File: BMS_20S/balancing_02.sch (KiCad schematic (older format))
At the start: 61 parts, among them Q2001 Si2302DS, Q2002 Si2302DS, Q3403 Si2302DS, Q3404 Si2302DS, U2004 TLP290-4

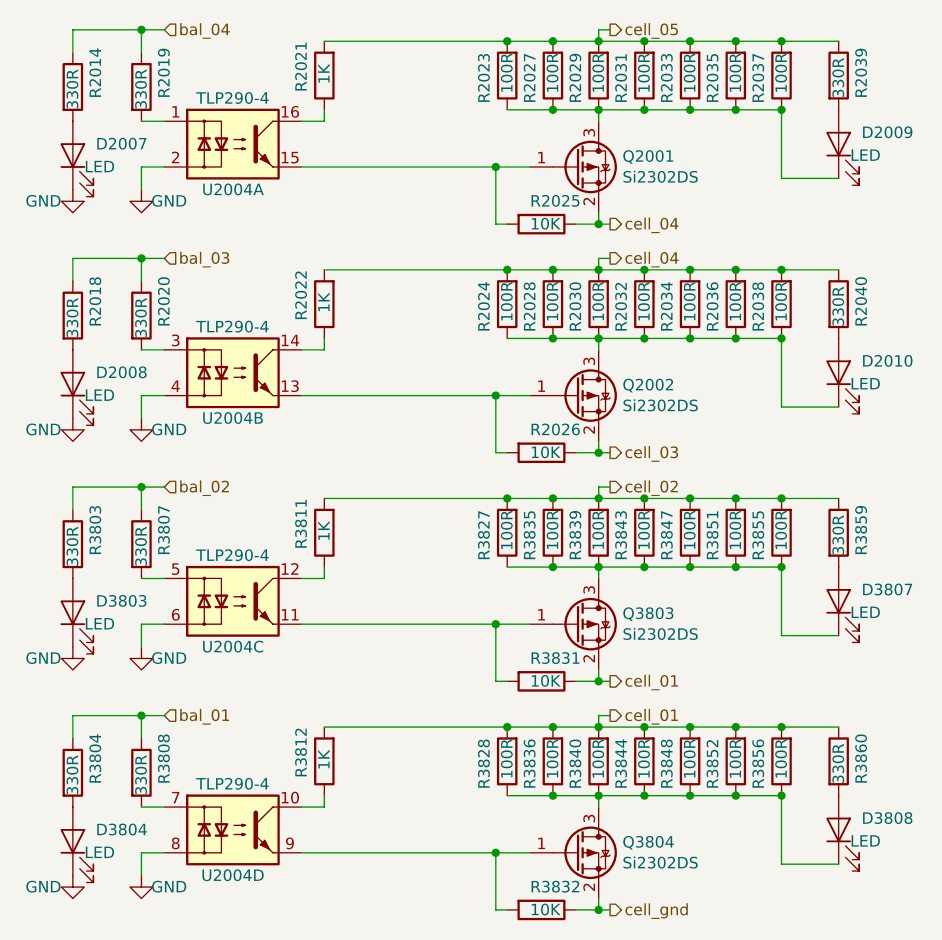
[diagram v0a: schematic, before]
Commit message: add current sense block to the schematic
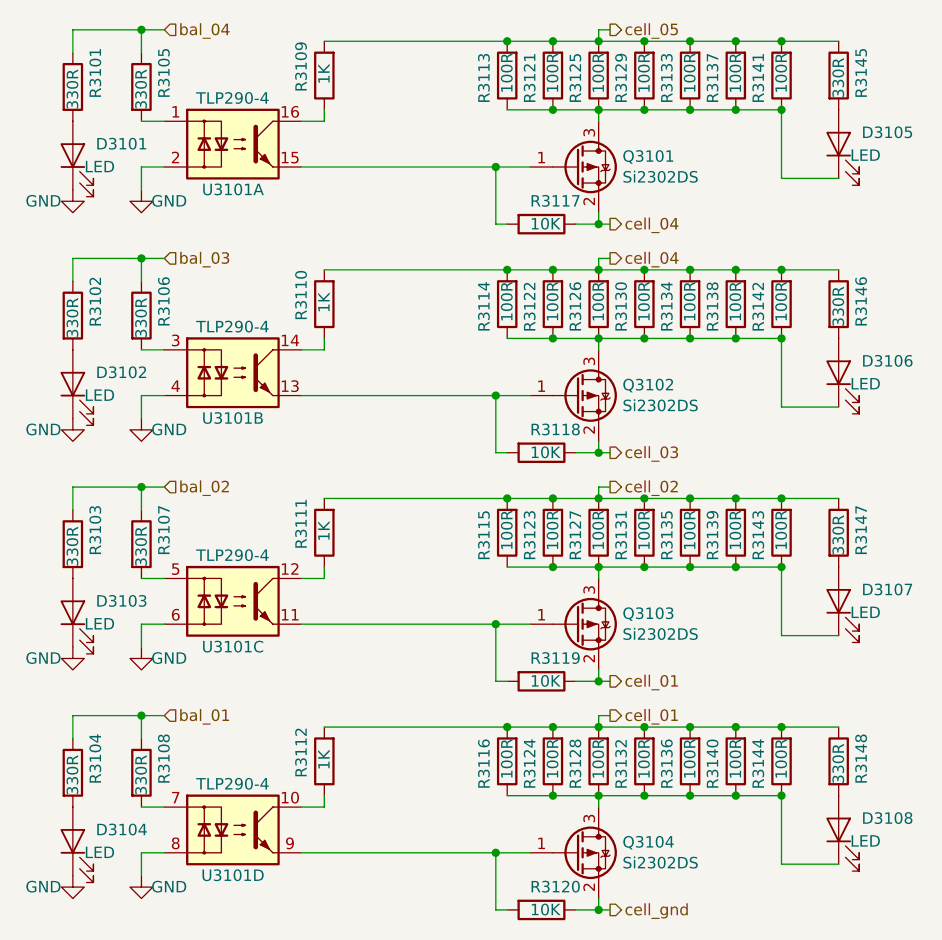
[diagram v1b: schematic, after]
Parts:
- renumbered D2007 to D3101, D2008 to D3102, D3403 to D3103, D3404 to D3104, D2009 to D3105, D2010 to D3106, D3407 to D3107, D3408 to D3108, Q2001 to Q3101, Q2002 to Q3102, Q3403 to Q3103, Q3404 to Q3104, R2014 to R3101, R2018 to R3102, R3403 to R3103, R3404 to R3104, R2019 to R3105, R2020 to R3106, R3407 to R3107, R3408 to R3108, R2021 to R3109, R2022 to R3110, R3411 to R3111, R3412 to R3112, R2023 to R3113, R2024 to R3114, R3427 to R3115, R3428 to R3116, R2025 to R3117, R2026 to R3118, R3431 to R3119, R1915 to R3120, R2027 to R3121, R2028 to R3122, R3435 to R3123, R3436 to R3124, R2029 to R3125, R2030 to R3126, R3439 to R3127, R3440 to R3128, R2031 to R3129, R2032 to R3130, R3443 to R3131, R3444 to R3132, R2033 to R3133, R2034 to R3134, R3447 to R3135, R3448 to R3136, R2035 to R3137, R2036 to R3138, R3451 to R3139, R3452 to R3140, R2037 to R3141, R2038 to R3142, R3455 to R3143, R3456 to R3144, R2039 to R3145, R2040 to R3146, R3459 to R3147, R3460 to R3148, U2004 to U3101
